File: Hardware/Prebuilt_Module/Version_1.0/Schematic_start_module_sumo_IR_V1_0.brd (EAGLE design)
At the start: 10.4 x 11.4 mm, 19 parts, among them IC1 ATTINY24,44,84_QFNVQFN

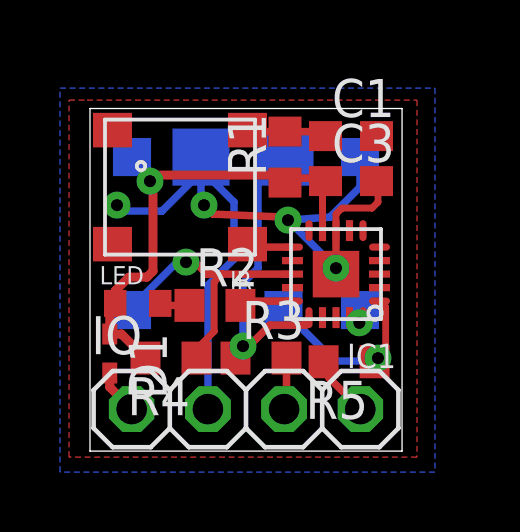
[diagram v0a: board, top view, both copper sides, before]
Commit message: Some corrections from 1.0
Due to some errors, I decided to switch to 0402 components, thus making
it easier to route and to add another feature: a serial resistor for
the home-pad. The signals for the pads used for the pogo-bead are
changed. The positions are still the same, but the signals are a little
mixed.
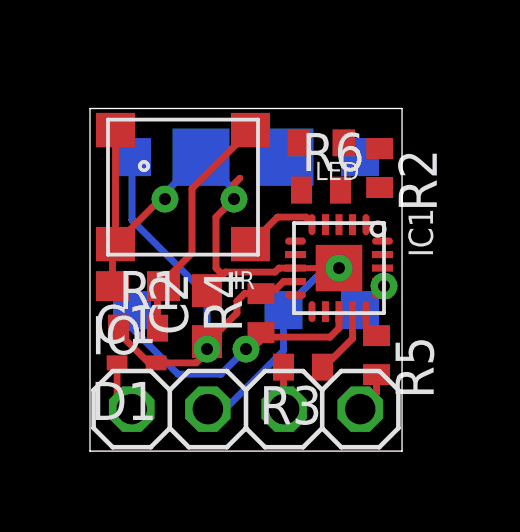
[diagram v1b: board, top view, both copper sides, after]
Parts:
- removed C3: 1uF, rcl:C0603
- added C2: 1uF, rcl:C0603
- added R6: 1k, rcl:R0402
- MISO_PAD: value (none) -> mosi
- MOSI_PAD: value mosi -> (none); device CRF:PAD_75X75 -> CRF:PAD_50X50
- R1, R2, R3, R4, R5: device rcl:R0603 -> rcl:R0402
- SCK_PAD: device CRF:PAD_50X50 -> CRF:PAD_75X75
- moved C1 8.68 mm to (1.60, 5.50), turned to 180 degrees
- moved LED 8.13 mm to (7.71, 10.3), turned to 180 degrees
- moved R1 7.52 mm to (1.60, 4.10), turned to 0 degrees
- moved R2 7.15 mm to (9.66, 9.44), turned to 270 degrees
- moved GND_PAD 5.70 mm to (6.45, 4.70)
- moved MOSI_PAD 5.68 mm to (9.00, 4.70)
- moved SCK_PAD 5.10 mm to (6.50, 9.80)
- moved MISO_PAD 5.10 mm to (9.00, 9.80), turned to 0 degrees
- moved R4 3.35 mm to (5.70, 4.60), turned to 90 degrees
- moved R3 1.43 mm to (7.10, 2.80), turned to 180 degrees
- moved D1 1.01 mm to (1.60, 2.94), turned to 180 degrees
- moved R5 0.94 mm to (9.55, 3.20), turned to 270 degrees
- moved IC1 0.22 mm to (8.30, 6.10), turned to 270 degrees
- moved IR 0.10 mm to (3.10, 8.80)
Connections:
- removed net LED: IC1.15, R2.2
- new net KILL: IC1.15, R5.1
- new net N$2: R6.1, SCK_PAD.P$1
- new net START: IC1.14, R3.1
- net GND: now also C2.2, LED.2; no longer C3.2
- net IR: now also IC1.5; no longer IC1.11
- net MISO: now also R2.2
- net MOSI: no longer R3.1
- net N$1: now also LED.1; no longer LED.2
- net SCK: now also R6.2; no longer R5.1, SCK_PAD.P$1
- net VCC: now also C2.1; no longer C3.1, LED.1
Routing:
- net MOSI: track 10.2 -> 1.45 mm
- net SCK: track 6.34 -> 0.00 mm, vias 1 -> 0
- net N$6: track 2.84 -> 7.88 mm
- net START: track 0.00 -> 2.29 mm
- net LED: track 1.95 -> 0.00 mm
- net GND: track 28.4 -> 26.7 mm, vias 4 -> 3
- net N$1: track 1.36 -> 0.00 mm
- net VCC: track 16.5 -> 15.5 mm
- net IR: track 1.54 -> 2.56 mm
- net KILL: track 0.00 -> 0.96 mm
- net MISO: track 0.68 -> 0.00 mm, vias 1 -> 0
- net KILL_SWITCH: track 2.04 -> 1.37 mm
- removed copper zone on layer 1, net GND
- removed copper zone on layer 16, net GND
